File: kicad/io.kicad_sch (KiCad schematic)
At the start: 10 parts, among them J12 LED stick, J5 IO 3x6 RA, U14 74AHCT1G125

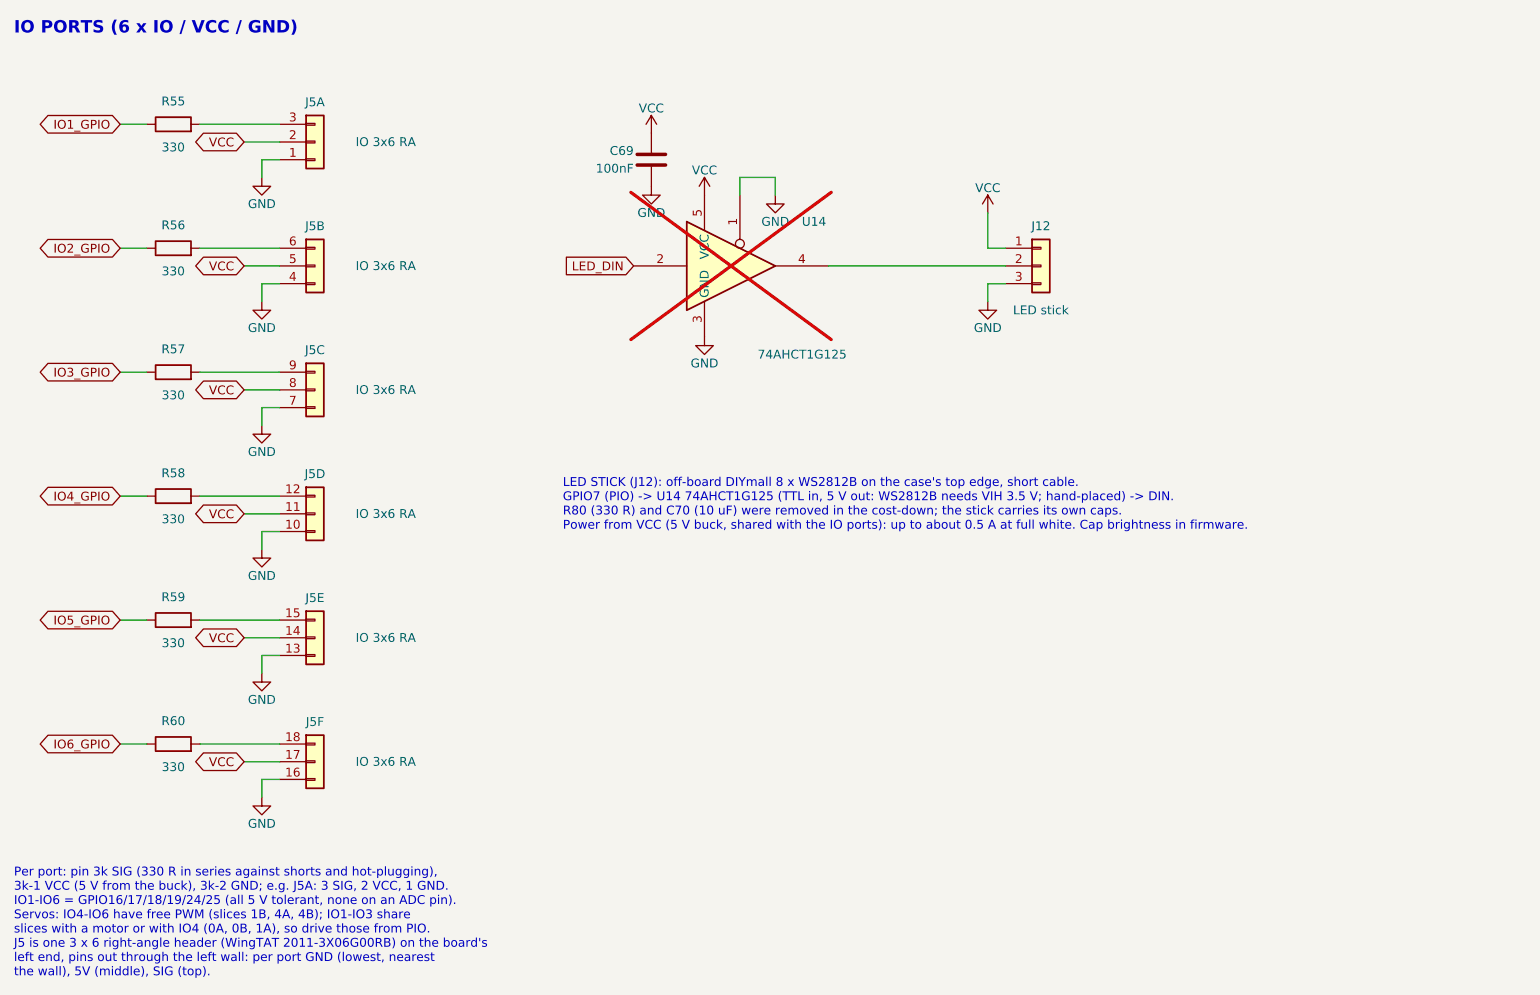
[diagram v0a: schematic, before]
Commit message: Rotate U10 to 0 deg and re-place the brain at 66.6 x 32 mm, unrouted
USB now runs straight down from J1 into U10's north pins; IO goes west to J5,
which moves to the top of the left wall with M5/M6 below it. SW1 sits under
U16 and SW2 in the bottom-right corner; Q1 is east of J3. GPIO map redone for
the new orientation (IO1-6 on GPIO0-3/8/9, motors on GPIO12-17/20-23/26-27,
USB-A on GPIO24/25, LED on GPIO29). ERC clean, DRC parity clean.

Co-Authored-By: Claude Opus 5.5 <noreply@anthropic.com>
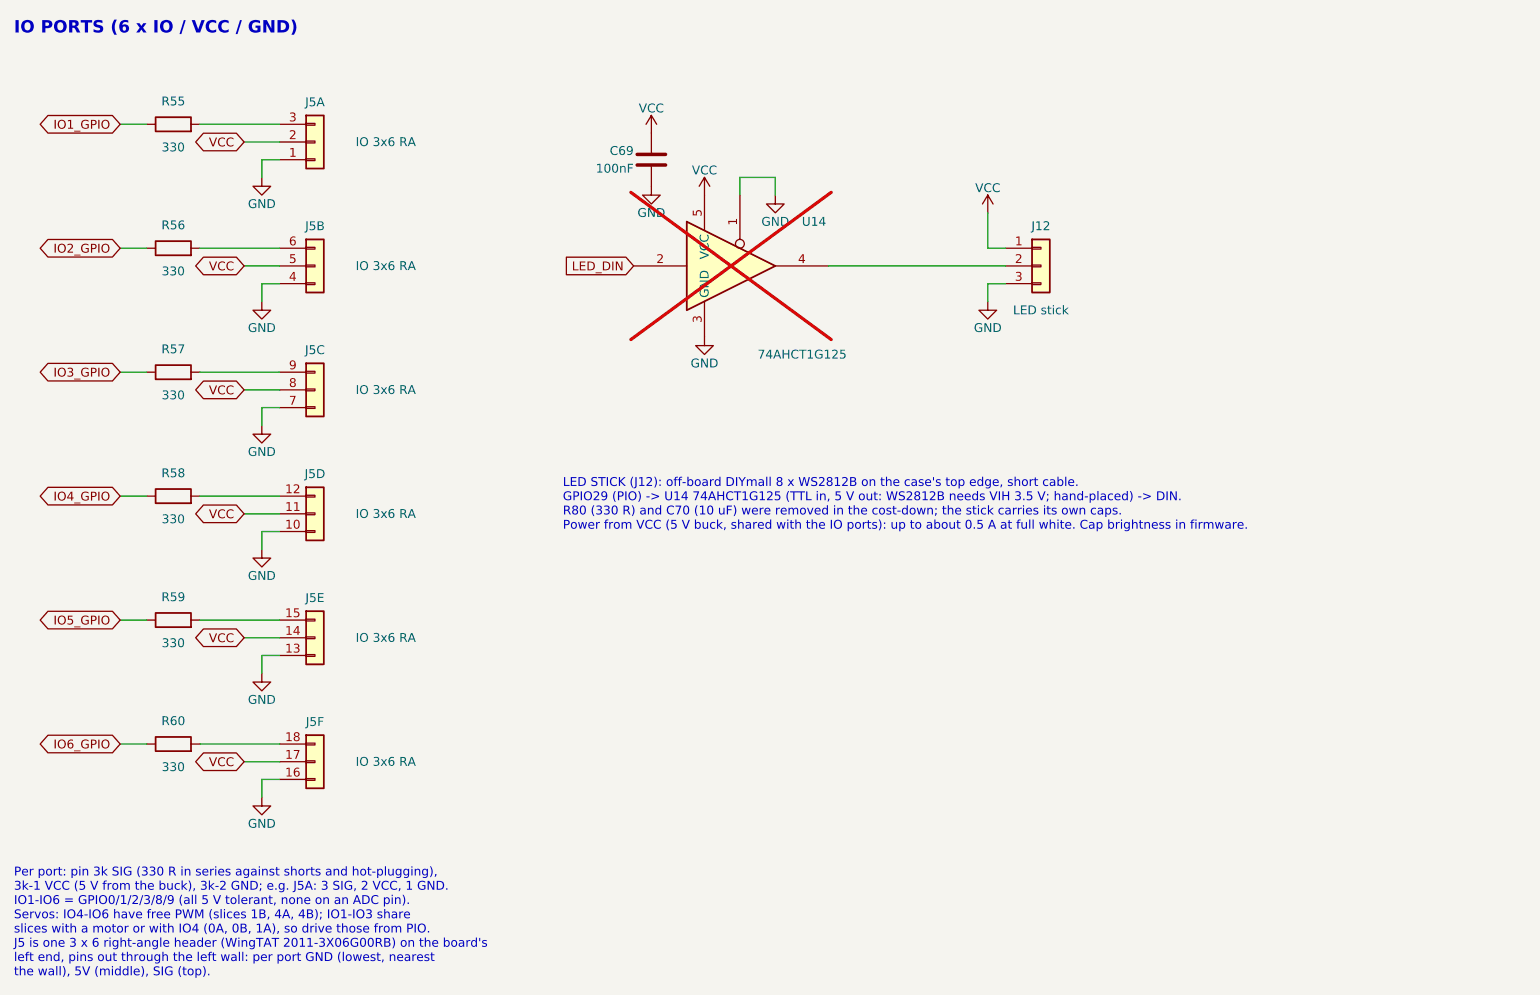
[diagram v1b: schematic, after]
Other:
- note added: "LED STICK (J12): off-board DIYmall 8 x WS2812B on the case's top edge, short cable. GPIO29 (PIO) -> U14 74AHCT1G125 (TTL in, 5 V out: WS2812B needs VIH 3.5 V; hand-placed) -> DIN. R80 (330 R) and C70 (10 uF) were removed in the cost-down; the stick carries its own caps. Power from VCC (5 V buck, shared with the IO ports): up to about 0.5 A at full white. Cap brightness in firmware."
- note added: "Per port: pin 3k SIG (330 R in series against shorts and hot-plugging), 3k-1 VCC (5 V from the buck), 3k-2 GND; e.g. J5A: 3 SIG, 2 VCC, 1 GND. IO1-IO6 = GPIO0/1/2/3/8/9 (all 5 V tolerant, none on an ADC pin). Servos: IO4-IO6 have free PWM (slices 1B, 4A, 4B); IO1-IO3 share slices with a motor or with IO4 (0A, 0B, 1A), so drive those from PIO. J5 is one 3 x 6 right-angle header (WingTAT 2011-3X06G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"
- note removed: "LED STICK (J12): off-board DIYmall 8 x WS2812B on the case's top edge, short cable. GPIO7 (PIO) -> U14 74AHCT1G125 (TTL in, 5 V out: WS2812B needs VIH 3.5 V; hand-placed) -> DIN. R80 (330 R) and C70 (10 uF) were removed in the cost-down; the stick carries its own caps. Power from VCC (5 V buck, shared with the IO ports): up to about 0.5 A at full white. Cap brightness in firmware."
- note removed: "Per port: pin 3k SIG (330 R in series against shorts and hot-plugging), 3k-1 VCC (5 V from the buck), 3k-2 GND; e.g. J5A: 3 SIG, 2 VCC, 1 GND. IO1-IO6 = GPIO16/17/18/19/24/25 (all 5 V tolerant, none on an ADC pin). Servos: IO4-IO6 have free PWM (slices 1B, 4A, 4B); IO1-IO3 share slices with a motor or with IO4 (0A, 0B, 1A), so drive those from PIO. J5 is one 3 x 6 right-angle header (WingTAT 2011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"
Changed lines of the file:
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@@
 	(generator_version "10.0")
 	(paper "A4")
-	(text "LED STICK (J12): off-board DIYmall 8 x WS2812B on the case's top edge, short cable.\nGPIO7 (PIO) -> U14 74AHCT1G125 (TTL in, 5 V out: WS2812B needs VIH 3.5 V; hand-placed) -> DIN.\nR80 (330 R) and C70 (10 uF) were removed in the cost-down; the stick carries its own caps.\nPower from VCC (5 V buck, shared with the IO ports): up to about 0.5 A at full white. Cap brightness in firmware."
+	(text "LED STICK (J12): off-board DIYmall 8 x WS2812B on the case's top edge, short cable.\nGPIO29 (PIO) -> U14 74AHCT1G125 (TTL in, 5 V out: WS2812B needs VIH 3.5 V; hand-placed) -> DIN.\nR80 (330 R) and C70 (10 uF) were removed in the cost-down; the stick carries its own caps.\nPower from VCC (5 V buck, shared with the IO ports): up to about 0.5 A at full white. Cap brightness in firmware."
 		(exclude_from_sim no)
 		(at 165.1 104.14 0)
@@
 		)
 	)
-	(text "Per port: pin 3k SIG (330 R in series against shorts and hot-plugging),\n3k-1 VCC (5 V from the buck), 3k-2 GND; e.g. J5A: 3 SIG, 2 VCC, 1 GND.\nIO1-IO6 = GPIO16/17/18/19/24/25 (all 5 V tolerant, none on an ADC pin).\nServos: IO4-IO6 have free PWM (slices 1B, 4A, 4B); IO1-IO3 share\nslices with a motor or with IO4 (0A, 0B, 1A), so drive those from PIO.\nJ5 is one 3 x 6 right-angle header (WingTAT 2011-3X06G00RB) on the board's\nleft end, pins out through the left wall: per port GND (lowest, nearest\nthe wall), 5V (middle), SIG (top)."
+	(text "Per port: pin 3k SIG (330 R in series against shorts and hot-plugging),\n3k-1 VCC (5 V from the buck), 3k-2 GND; e.g. J5A: 3 SIG, 2 VCC, 1 GND.\nIO1-IO6 = GPIO0/1/2/3/8/9 (all 5 V tolerant, none on an ADC pin).\nServos: IO4-IO6 have free PWM (slices 1B, 4A, 4B); IO1-IO3 share\nslices with a motor or with IO4 (0A, 0B, 1A), so drive those from PIO.\nJ5 is one 3 x 6 right-angle header (WingTAT 2011-3X06G00RB) on the board's\nleft end, pins out through the left wall: per port GND (lowest, nearest\nthe wall), 5V (middle), SIG (top)."
 		(exclude_from_sim no)
 		(at 86.36 152.4 0)

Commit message: Have JLC place SW2, D4, U14 and F2, and shift U8 onto its model
- SW2 (BOOT), D4, U14 and F2 were DNP for hand placement. All four are
  in stock at JLC, so they're placed now (DNP cleared in the schematic
  and on the board). The JLC BOM grows from 47 to 51 lines.
- fab.py: JLC's SOT-89-3 model for U8 (C16106) sits 0.474 mm toward the
  tab from its footprint origin, so U8's CPL point moves that far toward
  its pins (JLC_PART_SHIFT), replacing the pad-centre approximation.
- The 10-panel JLC quote is $331.69, and the preview shows all five parts
  correct.

Co-Authored-By: Claude Opus 5.5 <noreply@anthropic.com>
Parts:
- U14: now fitted
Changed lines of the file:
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@@
 		(on_board yes)
 		(in_pos_files yes)
-		(dnp yes)
+		(dnp no)
 		(property "Reference" "U14"
 			(at 199.39 59.69 0)
